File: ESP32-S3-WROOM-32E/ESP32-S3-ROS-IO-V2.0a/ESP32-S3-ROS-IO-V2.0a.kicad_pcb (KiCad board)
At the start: 2 copper layers, 96.7 x 100 mm, 45 parts, among them J1 Conn_01x22_Socket, J16 XT60-M, J17 XT60-M, J2 Conn_01x22_Socket, J3 Conn_01x22_Socket, J4 Conn_01x22_Socket, J5 Conn_01x02_Pin, SW1 SW1, SW2 SW2, SW3 SW3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

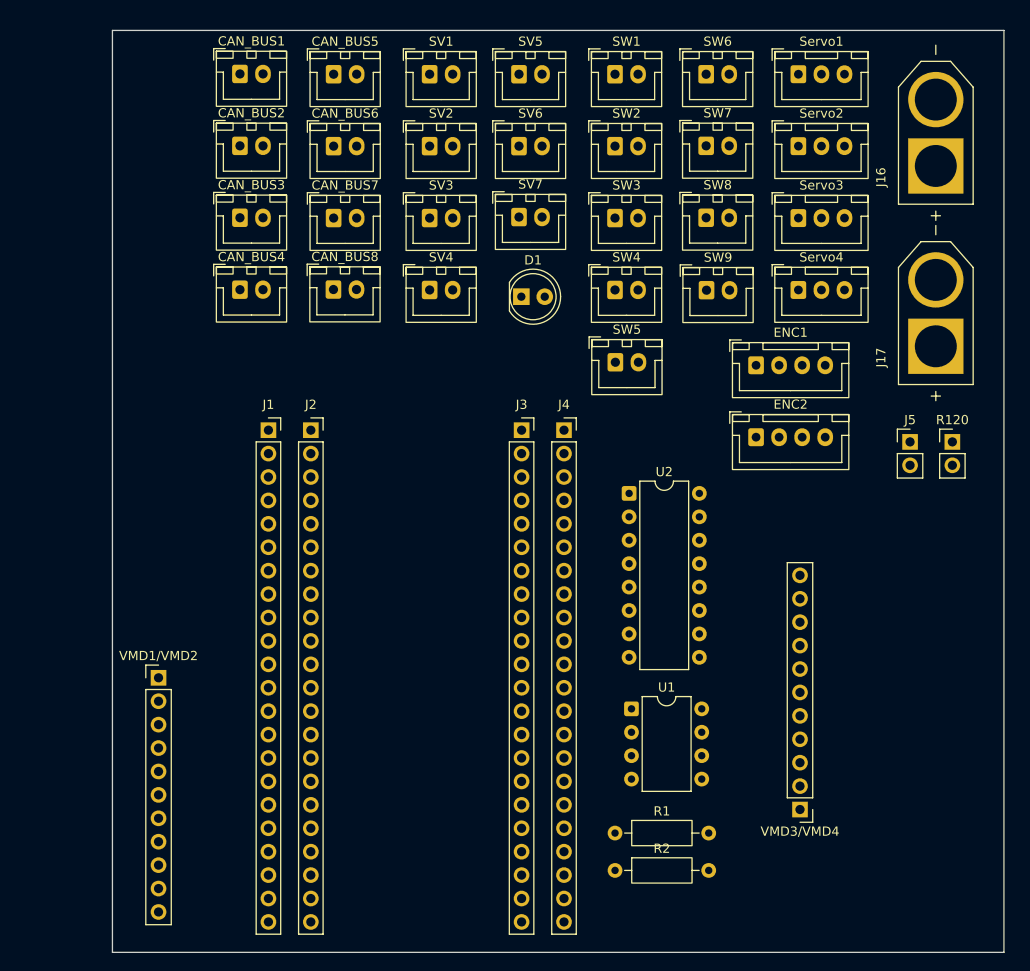
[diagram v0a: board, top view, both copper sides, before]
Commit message: アクチュエーター数変更
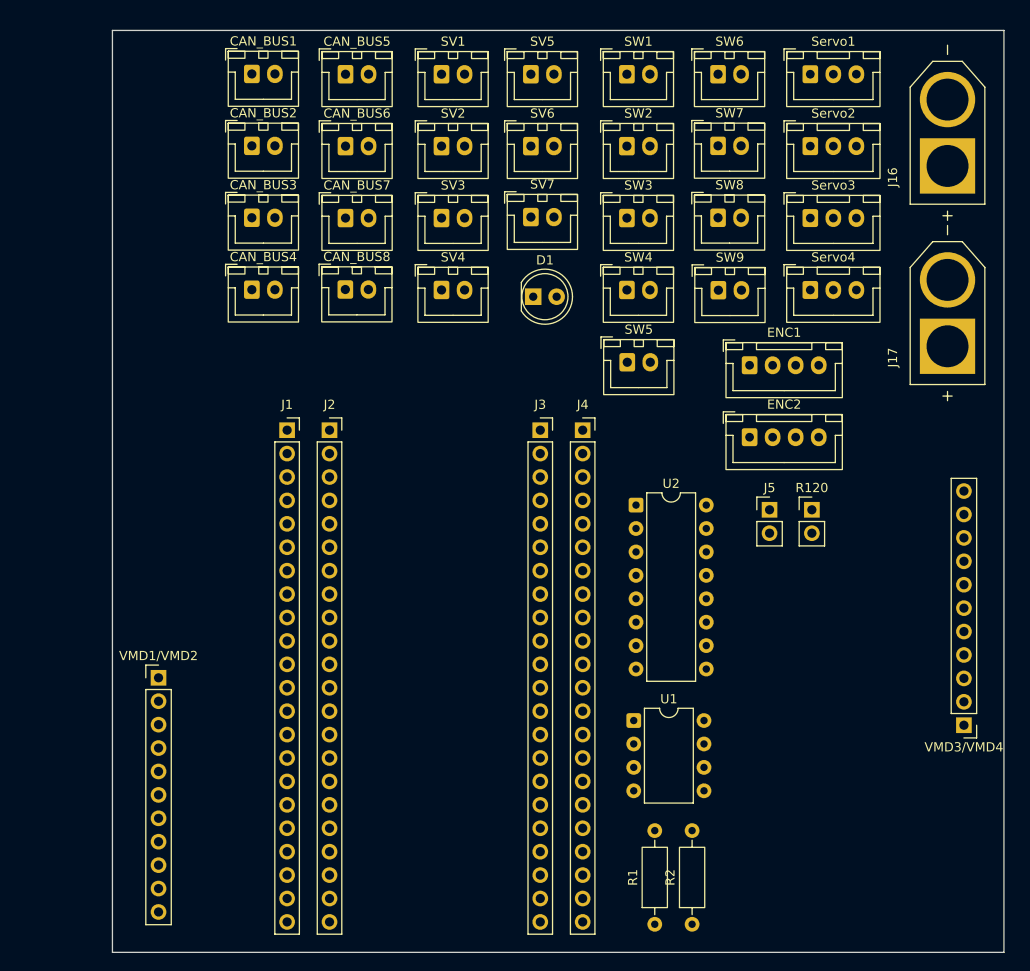
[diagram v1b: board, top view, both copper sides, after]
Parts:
- moved VMD3/VMD4 20.0 mm to (197.4, 118.4)
- moved J5 16.9 mm to (176.3, 95.0)
- moved R120 16.9 mm to (180.9, 95.0)
- moved R1 10.8 mm to (163.8, 140.0), turned to 90 degrees
- moved R2 10.2 mm to (167.9, 140.0), turned to 90 degrees
- moved J3 2.03 mm to (151.4, 86.4)
- moved J4 2.03 mm to (156.0, 86.4)
- moved J1 2.03 mm to (123.9, 86.4)
- moved J2 2.03 mm to (128.5, 86.4)
- moved U2 1.48 mm to (161.8, 94.5)
- moved U1 1.29 mm to (161.5, 117.9)
- moved CAN_BUS5 1.29 mm to (130.3, 47.8)
- moved CAN_BUS6 1.29 mm to (130.3, 55.6)
- moved CAN_BUS7 1.29 mm to (130.3, 63.4)
- moved SW5 1.29 mm to (160.8, 79.0)
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
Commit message: 一応ちゃんと配置
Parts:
- removed CAN_BUS5, CAN_BUS6, CAN_BUS7, CAN_BUS8: CAN_BUS, Connector_JST:JST_XH_B2B-XH-A_1x02_P2.50mm_Vertical
- removed J5: Conn_01x02_Pin, Connector_PinHeader_2.54mm:PinHeader_1x02_P2.54mm_Vertical
- removed SV7: SV7, Connector_JST:JST_XH_B2B-XH-A_1x02_P2.50mm_Vertical
- removed SW6: SW6, Connector_JST:JST_XH_B2B-XH-A_1x02_P2.50mm_Vertical
- removed SW7: SW7, Connector_JST:JST_XH_B2B-XH-A_1x02_P2.50mm_Vertical
- removed SW8: SW8, Connector_JST:JST_XH_B2B-XH-A_1x02_P2.50mm_Vertical
- removed SW9: SW9, Connector_JST:JST_XH_B2B-XH-A_1x02_P2.50mm_Vertical
- moved SW5 49.4 mm to (112.0, 86.5)
- moved SW3 49.4 mm to (112.0, 70.9)
- moved SW4 49.4 mm to (112.0, 78.7)
- moved SW1 49.2 mm to (112.0, 54.6)
- moved SW2 49.2 mm to (112.0, 62.4)
- moved Servo1 29.0 mm to (152.5, 54.4)
- moved Servo2 29.0 mm to (152.5, 62.2)
- moved Servo3 29.0 mm to (152.5, 70.0)
- moved Servo4 29.0 mm to (152.5, 77.8)
- moved SV5 28.5 mm to (132.5, 69.8)
- moved ENC1 26.4 mm to (165.2, 54.4)
- moved ENC2 26.4 mm to (165.2, 62.2)
- moved R120 26.4 mm to (172.7, 69.8)
- moved SV6 16.3 mm to (142.7, 69.8)
- moved D1 14.5 mm to (165.1, 71.1)
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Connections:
- U2 pad 10: O7 -> unconnected-(U2-O7-Pad10)
- U2 pad 7: TR7 -> unconnected-(U2-I7-Pad7)
- VMD1/VMD2 pad 11: MD1D/SW5/ENC3_A -> GPIO8
- VMD1/VMD2 pad 5: MD2P/SW2 -> GPIO5
- VMD1/VMD2 pad 7: MD2D/SW6/ENC3_B -> GPIO9
- VMD1/VMD2 pad 9: MD1P/SW1 -> GPIO4
- VMD3/VMD4 pad 11: MD3D/SW7/ENC4_A -> GPIO10
- VMD3/VMD4 pad 5: MD4P/SW4 -> GPIO7
- VMD3/VMD4 pad 7: MD4D/SW8/ENC4_B -> GPIO11
- VMD3/VMD4 pad 9: MD3P/SW3 -> GPIO6
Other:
- board size 96.7 x 100 mm -> 100 x 92 mm

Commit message: 配置
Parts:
- moved R120 13.7 mm to (184.2, 77.5), turned to 90 degrees
- moved VMD3/VMD4 3.81 mm to (185.4, 115.6)
- moved D1 3.17 mm to (167.6, 73.0)
- moved J17 0.63 mm to (185.4, 69.2)
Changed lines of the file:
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@@
 	(footprint "XT60-M:AMASS_XT60-M"
 		(layer "F.Cu")
-		(at 185.42 69.85)
+		(at 185.42 69.215)
 		(property "Reference" "J17"
 			(at -4.825 -5.935 0)
@@
 	(footprint "Connector_PinHeader_2.54mm:PinHeader_1x11_P2.54mm_Vertical"
 		(layer "F.Cu")
-		(at 185.42 111.76 180)
+		(at 185.42 115.57 180)
 		(descr "Through hole straight pin header, 1x11, 2.54mm pitch, single row")
 		(tags "Through hole pin header THT 1x11 2.54mm single row")
@@
 	(footprint "LED_THT:LED_D5.0mm"
 		(layer "F.Cu")
-		(at 165.1 71.12)
+		(at 167.64 73.025)
 		(descr "LED, diameter 5.0mm, 2 pins, http://cdn-reichelt.de/documents/datenblatt/A500/LL-504BC2E-009.pdf, generated by kicad-footprint-generator")
 		(tags "LED")
@@
 	(footprint "Connector_PinHeader_2.54mm:PinHeader_1x02_P2.54mm_Vertical"
 		(layer "F.Cu")
-		(at 172.72 69.85)
+		(at 184.15 77.47 90)
 		(descr "Through hole straight pin header, 1x02, 2.54mm pitch, single row")
 		(tags "Through hole pin header THT 1x02 2.54mm single row")
 		(property "Reference" "R120"
-			(at 0 -2.38 0)
+			(at 0 -2.38 90)
 			(layer "F.SilkS")
 			(effects
@@
 		)
 		(property "Value" "R120"
-			(at 0 4.92 0)
+			(at 0 4.92 90)
 			(layer "F.Fab")
 			(effects
@@
 		)
 		(property "Datasheet" "~"
-			(at 0 0 0)
+			(at 0 0 90)
 			(layer "F.Fab")
 			(hide yes)
@@
 		)
 		(property "Description" "Generic connector, single row, 01x02, script generated"
-			(at 0 0 0)
+			(at 0 0 90)
 			(layer "F.Fab")
 			(hide yes)
@@
 		)
 		(fp_line
-			(start -1.38 1.27)
-			(end -1.38 3.92)
+			(start 1.38 1.27)
+			(end 1.38 3.92)
 			(stroke
 				(width 0.12)
@@
 		)
 		(fp_line
-			(start -1.38 3.92)
-			(end 1.38 3.92)
+			(start -1.38 1.27)
+			(end -1.38 3.92)
 			(stroke
 				(width 0.12)
@@
 		)
 		(fp_line
-			(start 1.38 1.27)
+			(start -1.38 3.92)
 			(end 1.38 3.92)
 			(stroke
@@
 		)
 		(fp_line
-			(start -1.27 -0.635)
-			(end -0.635 -1.27)
+			(start 1.27 -1.27)
+			(end 1.27 3.81)
 			(stroke
 				(width 0.1)
@@
 		)
 		(fp_line
-			(start -1.27 3.81)
-			(end -1.27 -0.635)
+			(start -0.635 -1.27)
+			(end 1.27 -1.27)
 			(stroke
 				(width 0.1)
@@
 		)
 		(fp_line
-			(start -0.635 -1.27)
-			(end 1.27 -1.27)
+			(start -1.27 -0.635)
+			(end -0.635 -1.27)
 			(stroke
 				(width 0.1)
@@
 		)
 		(fp_line
-			(start 1.27 -1.27)
-			(end 1.27 3.81)
+			(start 1.27 3.81)
+			(end -1.27 3.81)
 			(stroke
 				(width 0.1)
@@
 		)
 		(fp_line
-			(start 1.27 3.81)
-			(end -1.27 3.81)
+			(start -1.27 3.81)
+			(end -1.27 -0.635)
 			(stroke
 				(width 0.1)
@@
 		)
 		(fp_text user "${REFERENCE}"
-			(at 0 1.27 90)
+			(at 0 1.27 0)
 			(layer "F.Fab")
 			(effects
@@
 		)
 		(pad "1" thru_hole rect
-			(at 0 0)
+			(at 0 0 90)
 			(size 1.7 1.7)
 			(drill 1)
@@
 		)
 		(pad "2" thru_hole circle
-			(at 0 2.54)
+			(at 0 2.54 90)
 			(size 1.7 1.7)
 			(drill 1)

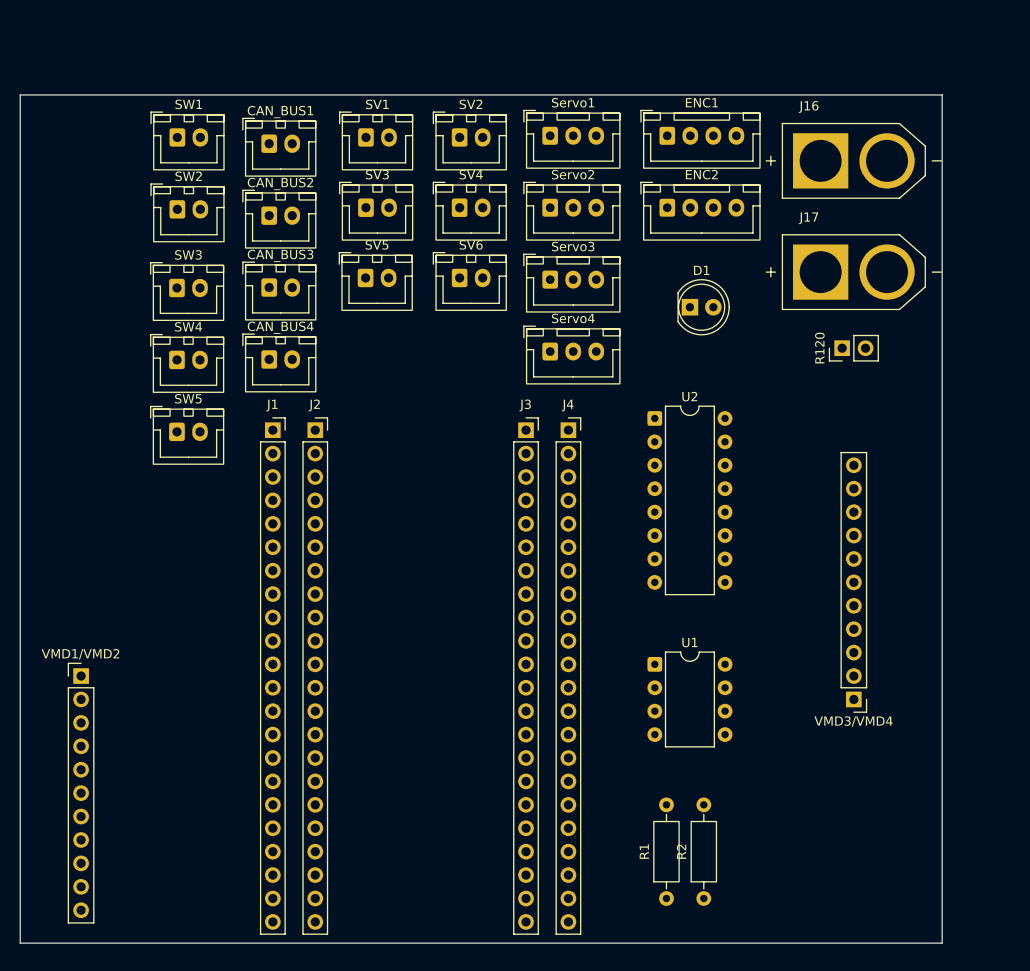
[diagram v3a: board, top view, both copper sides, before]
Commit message: 旧MD配置決めシルク完了１
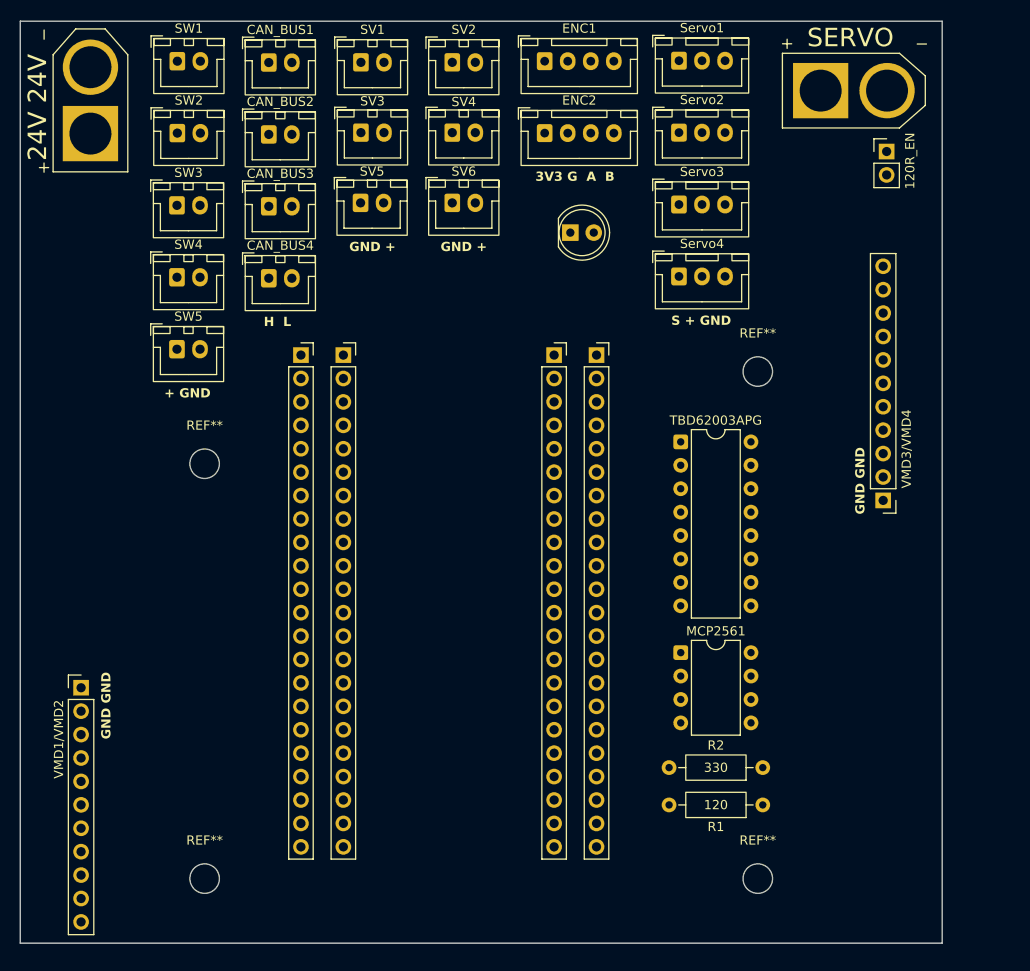
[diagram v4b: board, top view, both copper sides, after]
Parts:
- added REF**: MountingHole_3.2mm_M3, MountingHole:MountingHole_3.2mm_M3, F.Cu at (115.0, 90.0)
- added REF**: MountingHole_3.2mm_M3, MountingHole:MountingHole_3.2mm_M3, F.Cu at (115.0, 135.0)
- added REF**: MountingHole_3.2mm_M3, MountingHole:MountingHole_3.2mm_M3, F.Cu at (175.0, 135.0)
- added REF**: MountingHole_3.2mm_M3, MountingHole:MountingHole_3.2mm_M3, F.Cu at (175.0, 80.0)
- moved J17 84.9 mm to (102.6, 50.6), turned to 90 degrees
- moved R120 21.9 mm to (189.0, 56.1), turned to 0 degrees
- moved VMD3/VMD4 21.8 mm to (188.6, 94.0)
- moved Servo1 16.2 mm to (166.4, 46.3)
- moved Servo3 16.2 mm to (166.4, 61.9)
- moved Servo2 16.2 mm to (166.4, 54.1)
- moved Servo4 16.2 mm to (166.4, 69.7)
- moved R2 15.6 mm to (175.5, 123.0), turned to 180 degrees
- moved ENC1 15.6 mm to (151.9, 46.3)
- moved ENC2 15.6 mm to (151.9, 54.1)
- moved D1 15.3 mm to (154.7, 64.9)
- moved R1 14.6 mm to (175.5, 127.0), turned to 180 degrees
- moved SW5 8.96 mm to (112.0, 77.6)
- moved SW3 8.96 mm to (112.0, 62.0)
- moved SW4 8.96 mm to (112.0, 69.8)
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- renumbered U1 to MCP2561, U2 to TBD62003APG
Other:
- board size 100 x 92 mm -> 100 x 100 mm
- board text added: "+ GND"
- board text added: "120R_EN"
- board text added: "24V 24V"
- board text added: "3V3 G A B"
- board text added: "GND +"
- board text added: "GND GND"
- board text added: "H L"
- board text added: "S + GND"
- board text added: "SERVO"

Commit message: 旧MD配置決めシルク完了２
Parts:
- added G***6: LOGO, LOGO, F.Cu at (162.4, 93.6)
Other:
- board text added: "ESP32-S3-IO-Board-V2.0a 2026, NHK-Project, RRST"
- board text added: "USB"

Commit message: 製造ファイル出力
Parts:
- moved R120 2.54 mm to (190.5, 58.2)
- moved J16 0.76 mm to (185.4, 50.3)
- renumbered REF** to REF**1, REF** to REF**2, REF** to REF**3, REF** to REF**4, MCP2561 to U1, TBD62003APG to U2
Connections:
- ENC1 pad 1: 5VD -> 5V0
- ENC2 pad 1: 5VD -> 5V0
- J1 pad 21: 5VD -> 5V0
- J2 pad 21: 5VD -> 5V0
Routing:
- net CANL: track 0.00 -> 164.8 mm, vias 0 -> 2
- net CANH: track 0.00 -> 160.1 mm, vias 0 -> 1
- net +24V: track 0.00 -> 155.1 mm, vias 0 -> 1
- net 5V0: track 0.00 -> 123.8 mm, vias 0 -> 1
- net ENC1_B: track 0.00 -> 108.4 mm, vias 0 -> 1
- net GPIO35: track 0.00 -> 107.2 mm, vias 0 -> 1
- net GPIO10: track 0.00 -> 105.6 mm, vias 0 -> 1
- net ENC1_A: track 0.00 -> 105.1 mm, vias 0 -> 1
- net GPIO11: track 0.00 -> 99.6 mm, vias 0 -> 1
- net ENC2_A: track 0.00 -> 99.5 mm, vias 0 -> 1
- net GPIO36: track 0.00 -> 96.8 mm, vias 0 -> 1
- net GPIO16: track 0.00 -> 91.8 mm, vias 0 -> 1
- net GPIO37: track 0.00 -> 83.7 mm, vias 0 -> 1
- net O2: track 0.00 -> 82.6 mm, vias 0 -> 1
- net GPIO17: track 0.00 -> 82.2 mm, vias 0 -> 1
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- added copper zone on B.Cu, net GND
- added copper zone on F.Cu, net GND
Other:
- outline, holes or cut-outs redrawn
- board text added: "5V0 G A B"
- board text removed: "3V3 G A B"
